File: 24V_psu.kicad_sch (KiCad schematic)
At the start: 26 parts, among them J1 AC_IN, J2 DC_OUT, Q1 TIP122, Q2 BC546B

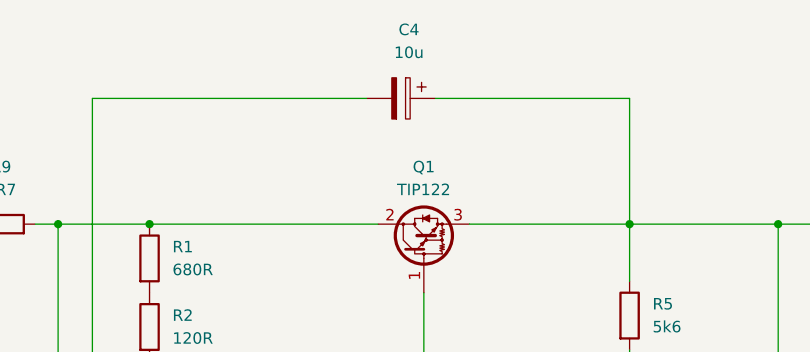
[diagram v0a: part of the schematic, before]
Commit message: Change C4 footprint to non-polarized
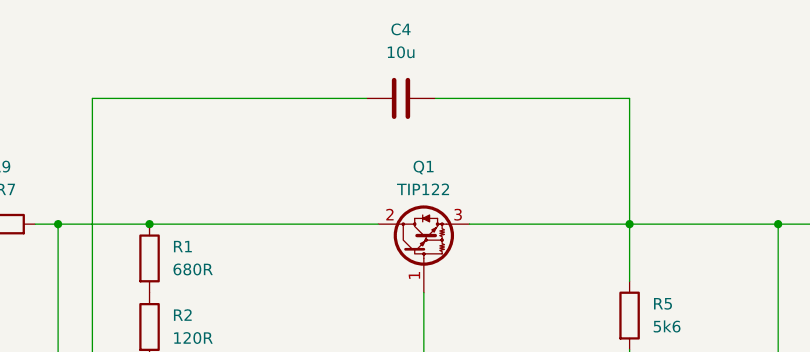
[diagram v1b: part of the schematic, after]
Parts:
- C4: footprint Capacitor_THT:CP_Radial_D5.0mm_P2.00mm -> Capacitor_THT:C_Radial_D5.0mm_H11.0mm_P2.00mm; symbol Device:C_Polarized -> Device:C
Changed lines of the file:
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@@
 (kicad_sch
-	(version 20231120)
+	(version 20250114)
 	(generator "eeschema")
-	(generator_version "8.0")
+	(generator_version "9.0")
 	(paper "A4")
 	(junction
@@
 	)
 	(symbol
-		(lib_id "Device:C_Polarized")
+		(lib_id "Device:C")
 		(at 129.54 49.53 270)
 		(unit 1)
@@
 		(fields_autoplaced yes)
 		(property "Reference" "C4"
-			(at 130.429 41.91 90)
+			(at 129.54 41.91 90)
 			(effects
 				(font
@@
 		)
 		(property "Value" "10u"
-			(at 130.429 44.45 90)
-			(effects
-				(font
-					(size 1.27 1.27)
-				)
-			)
-		)
-		(property "Footprint" "Capacitor_THT:CP_Radial_D5.0mm_P2.00mm"
+			(at 129.54 44.45 90)
+			(effects
+				(font
+					(size 1.27 1.27)
+				)
+			)
+		)
+		(property "Footprint" "Capacitor_THT:C_Radial_D5.0mm_H11.0mm_P2.00mm"
 			(at 125.73 50.4952 0)
 			(effects
@@
 			)
 		)
-		(property "Description" "Polarized capacitor"
+		(property "Description" "Unpolarized capacitor"
 			(at 129.54 49.53 0)
 			(effects
@@
 		)
 	)
+	(embedded_fonts no)
 )

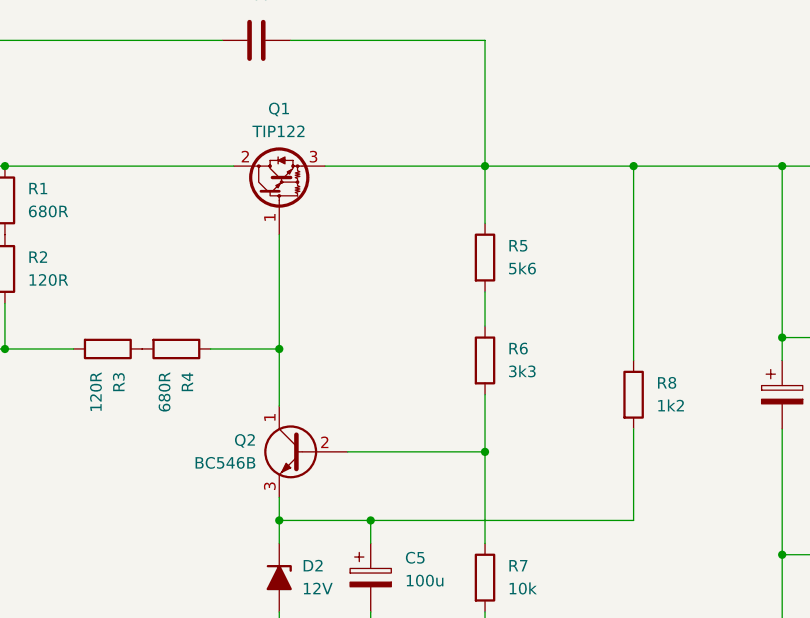
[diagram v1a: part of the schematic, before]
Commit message: Add C8 for slightly improved ripple rejection
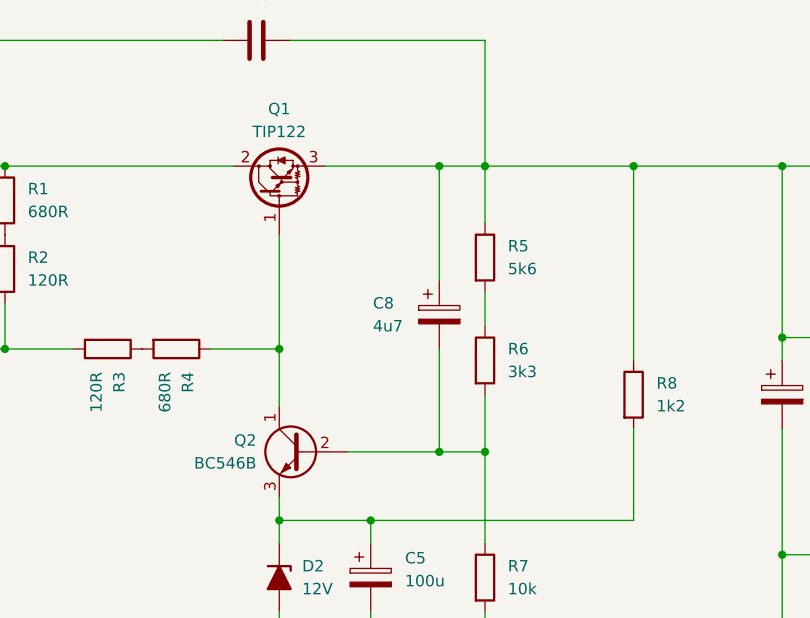
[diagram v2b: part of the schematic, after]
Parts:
- added C8: 4u7, Capacitor_THT:CP_Radial_D4.0mm_P2.00mm, symbol Device:C_Polarized
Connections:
- net V_OUT: now also C8.1
- net at Q2.2 (B), R6.2, R7.1: now also C8.2
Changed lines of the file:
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@@
 	(paper "A4")
+	(junction
+		(at 149.86 95.25)
+		(diameter 0)
+		(color 0 0 0 0)
+	)
 	(junction
 		(at 132.08 83.82)
@@
 	)
 	(junction
+		(at 149.86 63.5)
+		(diameter 0)
+		(color 0 0 0 0)
+	)
+	(junction
 		(at 132.08 116.84)
 		(diameter 0)
@@
 	(wire
 		(pts
+			(xy 149.86 83.82) (xy 149.86 95.25)
+		)
+		(stroke
+			(width 0)
+			(type default)
+		)
+	)
+	(wire
+		(pts
 			(xy 171.45 92.71) (xy 171.45 102.87)
 		)
@@
 	(wire
 		(pts
+			(xy 149.86 95.25) (xy 154.94 95.25)
+		)
+		(stroke
+			(width 0)
+			(type default)
+		)
+	)
+	(wire
+		(pts
 			(xy 74.93 116.84) (xy 80.01 116.84)
 		)
@@
 	(wire
 		(pts
+			(xy 149.86 63.5) (xy 149.86 76.2)
+		)
+		(stroke
+			(width 0)
+			(type default)
+		)
+	)
+	(wire
+		(pts
 			(xy 132.08 100.33) (xy 132.08 102.87)
 		)
@@
 	(wire
 		(pts
-			(xy 139.7 95.25) (xy 154.94 95.25)
+			(xy 139.7 95.25) (xy 149.86 95.25)
 		)
 		(stroke
@@
 	(wire
 		(pts
-			(xy 154.94 63.5) (xy 137.16 63.5)
+			(xy 154.94 63.5) (xy 149.86 63.5)
 		)
 		(stroke
@@
 		(pts
 			(xy 142.24 116.84) (xy 142.24 113.03)
+		)
+		(stroke
+			(width 0)
+			(type default)
+		)
+	)
+	(wire
+		(pts
+			(xy 149.86 63.5) (xy 137.16 63.5)
 		)
 		(stroke
@@
 					(unit 1)
 				)
+			)
+		)
+	)
+	(symbol
+		(lib_id "Device:C_Polarized")
+		(at 149.86 80.01 0)
+		(unit 1)
+		(exclude_from_sim no)
+		(in_bom yes)
+		(on_board yes)
+		(dnp no)
+		(property "Reference" "C8"
+			(at 142.494 78.74 0)
+			(effects
+				(font
+					(size 1.27 1.27)
+				)
+				(justify left)
+			)
+		)
+		(property "Value" "4u7"
+			(at 142.494 81.28 0)
+			(effects
+				(font
+					(size 1.27 1.27)
+				)
+				(justify left)
+			)
+		)
+		(property "Footprint" "Capacitor_THT:CP_Radial_D4.0mm_P2.00mm"
+			(at 150.8252 83.82 0)
+			(effects
+				(font
+					(size 1.27 1.27)
+				)
+				(hide yes)
+			)
+		)
+		(property "Datasheet" "~"
+			(at 149.86 80.01 0)
+			(effects
+				(font
+					(size 1.27 1.27)
+				)
+				(hide yes)
+			)
+		)
+		(property "Description" "Polarized capacitor"
+			(at 149.86 80.01 0)
+			(effects
+				(font
+					(size 1.27 1.27)
+				)
+				(hide yes)
+			)
+		)
+		(pin "2"
+		)
+		(pin "1"
+		)
+		(instances
+			(project "24V_psu"
+				(path "/d0d85e8f-075b-4eda-8b1d-04d0d1717e31"
+					(reference "C8")
+					(unit 1)
+				)

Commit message: Change J1 and J2 to 5mm pitch
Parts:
- J1, J2: footprint TerminalBlock_TE-Connectivity:TerminalBlock_TE_282834-2_1x02_P2.54mm_Horizontal -> TerminalBlock:TerminalBlock_MaiXu_MX126-5.0-02P_1x02_P5.00mm
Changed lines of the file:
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@@
 			)
 		)
-		(property "Footprint" "TerminalBlock_TE-Connectivity:TerminalBlock_TE_282834-2_1x02_P2.54mm_Horizontal"
+		(property "Footprint" "TerminalBlock:TerminalBlock_MaiXu_MX126-5.0-02P_1x02_P5.00mm"
 			(at 62.23 142.24 0)
 			(effects
@@
 			)
 		)
-		(property "Footprint" "TerminalBlock_TE-Connectivity:TerminalBlock_TE_282834-2_1x02_P2.54mm_Horizontal"
+		(property "Footprint" "TerminalBlock:TerminalBlock_MaiXu_MX126-5.0-02P_1x02_P5.00mm"
 			(at 115.57 138.43 0)
 			(effects

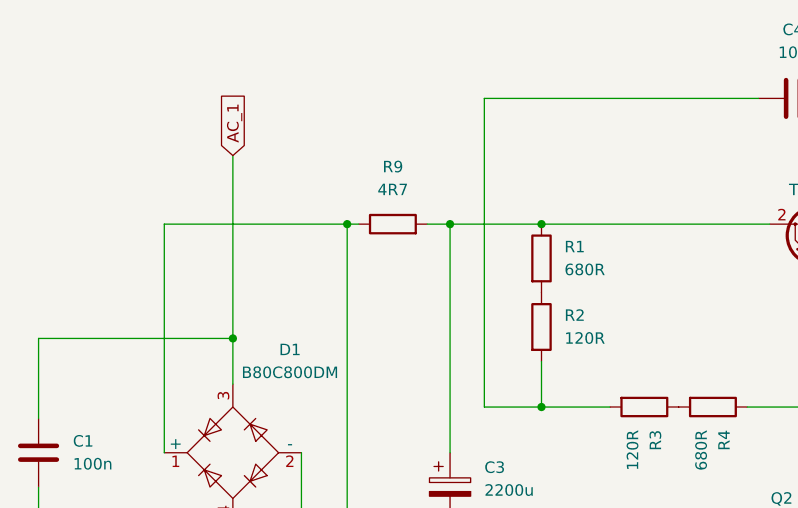
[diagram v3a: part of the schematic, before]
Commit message: Rotate R9 around
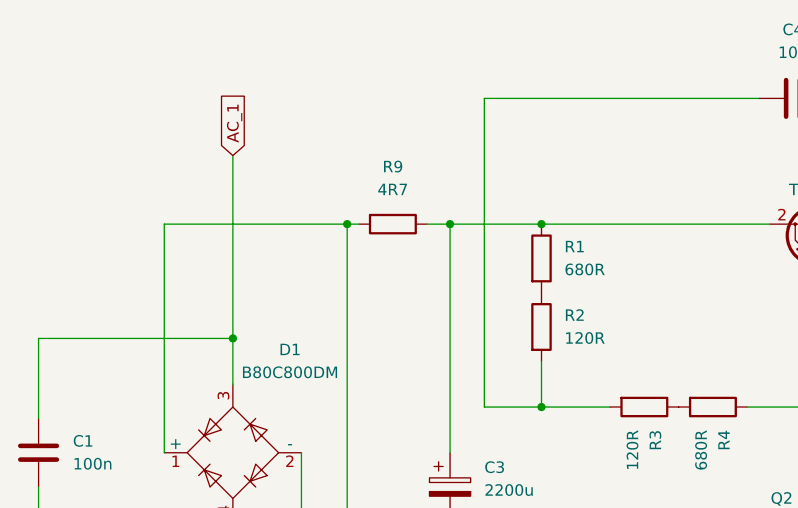
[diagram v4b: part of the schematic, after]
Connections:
- net at C2.1, D1.1 (+): now also R9.2; no longer R9.1
- net at C3.1, Q1.2 (C), R1.1: now also R9.1; no longer R9.2
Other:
- moved on the sheet: R9
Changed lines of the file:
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@@
 	(symbol
 		(lib_id "Device:R")
-		(at 85.09 63.5 90)
+		(at 85.09 63.5 270)
 		(unit 1)
 		(exclude_from_sim no)
@@
 		)
 		(property "Footprint" "Resistor_THT:R_Axial_DIN0414_L11.9mm_D4.5mm_P5.08mm_Vertical"
-			(at 85.09 65.278 90)
+			(at 85.09 61.722 90)
 			(effects
 				(font
